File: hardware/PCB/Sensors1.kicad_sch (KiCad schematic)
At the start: 33 parts, among them J10 Conn_ACS712, U1 MCP6002T-I/SN, U102 INA333xxDGK, U201 QNHC3, U6 ACS712xLCTR-05B, U7 TLV431, U8 TLV431

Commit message: Rough Layout pcb
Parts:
- removed JP201: SolderJumper_2_Open, Jumper:SolderJumper-2_P1.3mm_Open_TrianglePad1.0x1.5mm, symbol Jumper:SolderJumper_2_Open
- removed U7: TLV431, Package_TO_SOT_SMD:SOT-23, symbol Reference_Voltage:REF3012
- added C202, C208: 100n, Capacitor_SMD:C_0805_2012Metric, symbol Device:C
- added R205, R213: 4.7k, Resistor_SMD:R_0805_2012Metric, symbol Device:R
- added TP201, TP202, TP203, TP204, TP205, TP206, TP207: TestPoint, TestPoint:TestPoint_Pad_D1.5mm, symbol Connector:TestPoint
- added U205: TLV431, Package_TO_SOT_SMD:SOT-23, symbol Reference_Voltage:REF3012
- C203: renamed from C9; JLCPCB Part (none) -> C28323; Link (none) -> https://jlcpcb.com/partdetail/29074-CL21B105KBFNNNE/C28323
- C209: renamed from C8; JLCPCB Part (none) -> C28323; Link (none) -> https://jlcpcb.com/partdetail/29074-CL21B105KBFNNNE/C28323
- J201: renamed from U203; value ~ -> ina333; footprint (none) -> footprints:board_ina333; Link (none) -> https://pl.aliexpress.com/item/1005006230563668.html?spm=a2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; now left out of the parts list
- J202: renamed from J10; value Conn_ACS712 -> ACS712; footprint (none) -> Connector_PinHeader_2.54mm:PinHeader_1x03_P2.54mm_Vertical; Link (none) -> https://pl.aliexpress.com/item/1005006207760044.html?spm=a2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; now left out of the parts list
- R202: renamed from R22; JLCPCB Part (none) -> C38522; Link (none) -> https://jlcpcb.com/partdetail/39505-0805W8F1002T5E/C38522
- R204: renamed from R12; now not fitted
- R206: renamed from R14; JLCPCB Part (none) -> C38522; Link (none) -> https://jlcpcb.com/partdetail/39505-0805W8F1002T5E/C38522
- R208: renamed from R25; JLCPCB Part (none) -> C38522; Link (none) -> https://jlcpcb.com/partdetail/39505-0805W8F1002T5E/C38522
- R211: renamed from R23; JLCPCB Part (none) -> C38522; Link (none) -> https://jlcpcb.com/partdetail/39505-0805W8F1002T5E/C38522
- R216: renamed from R20; JLCPCB Part (none) -> C38522; Link (none) -> https://jlcpcb.com/partdetail/39505-0805W8F1002T5E/C38522
- U201: renamed from U102; JLCPCB Part (none) -> C2057648; Link (none) -> https://jlcpcb.com/partdetail/TexasInstruments-INA333AIDGKT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; MFR Part (none) -> INA333AIDGKT; Manufacturer (none) -> Texas Instruments
- renumbered C7 to C201, C5 to C204, C6 to C205, C1 to C206, C3 to C207, C4 to C210, JP1 to JP202, R11 to R201, R9 to R203, R6 to R207, R10 to R209, R19 to R210, R16 to R212, R13 to R214, R17 to R215, R18 to R217, U1 to U202, U8 to U203, U201 to U204, U6 to U206
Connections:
- net +3V3: no longer J201.3 (3V3)
- net +5V: now also C206.2, J201.3 (3V3); no longer C206.1
- net ACS712_out: now also TP205.1
- net Current_offset_1V5: now also TP206.1, U205.2 (OUT)
- net Current_opamp_V+: no longer R210.2, R212.2, U202.6 (-)
- net GND: now also C203.1, C205.1, C206.1, R208.1, U201.5 (Ref), C202.2, C208.2, U205.3 (GND); no longer C203.2, C205.2, C206.2, R208.2
- net QNHC3_out: now also TP204.1
- net ina333_Vin-: now also C205.2; no longer C205.1
- net ina333_Vout: now also C202.1, R205.2, TP203.1; no longer R201.1, U202.1
- net ina333_Vout_5V: now also TP201.1
- net ina333_Vref: no longer U201.5 (Ref)
- net ina333_offset_2V48: now also C203.2, R206.2, U203.2 (OUT), TP202.1; no longer C203.1, R206.1, U203.1 (IN)
- net ina333_opamp_V+: no longer R201.2, R203.2, U202.2 (-)
- net at R214.2, R216.1: now also U205.1 (REF)
- net QNH_out renamed Current_Vout
- net Current_Vout: now also R213.1
- new net: R206.1, R208.2, U203.1 (REF)
- new net Current_opamp_V-: R210.2, R212.2, U202.6 (-)
- new net QNH_Vout: C208.1, R213.2, TP207.1
- new net ina333_Vout_: R201.1, R205.1, U202.1
- new net ina333_opamp_V-: R201.2, R203.2, U202.2 (-)
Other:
- moved on the sheet: C203, C205, C209, R201, R202, R203, R206, R207, R208, R209, R210, R211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

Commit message: pcb XL4015
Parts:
- C203, C209: Distributor https://jlcpcb.com/partdetail/29074-CL21B105KBFNNNE/C28323 -> (none)
- R202, R206, R208, R211, R216: Distributor https://jlcpcb.com/partdetail/18102-0805W8F1002T5E/C17414 -> (none); Link https://jlcpcb.com/partdetail/39505-0805W8F1002T5E/C38522 -> https://jlcpcb.com/partdetail/18102-0805W8F1002T5E/C17414
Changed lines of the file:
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@@
 			)
 		)
-		(property "Distributor" "https://jlcpcb.com/partdetail/18102-0805W8F1002T5E/C17414"
-			(at 171.45 39.37 0)
-			(effects
-				(font
-					(size 1.27 1.27)
-				)
-				(hide yes)
-			)
-		)
 		(property "MFR Part" "0805W8F1002T5E "
 			(at 171.45 39.37 0)
@@
 			)
 		)
-		(property "Link" "https://jlcpcb.com/partdetail/39505-0805W8F1002T5E/C38522"
+		(property "Link" "https://jlcpcb.com/partdetail/18102-0805W8F1002T5E/C17414"
 			(at 171.45 39.37 0)
 			(effects
@@
 			)
 		)
-		(property "Distributor" "https://jlcpcb.com/partdetail/18102-0805W8F1002T5E/C17414"
-			(at 160.02 30.48 0)
-			(effects
-				(font
-					(size 1.27 1.27)
-				)
-				(hide yes)
-			)
-		)
 		(property "MFR Part" "0805W8F1002T5E "
 			(at 160.02 30.48 0)
@@
 			)
 		)
-		(property "Link" "https://jlcpcb.com/partdetail/39505-0805W8F1002T5E/C38522"
+		(property "Link" "https://jlcpcb.com/partdetail/18102-0805W8F1002T5E/C17414"
 			(at 160.02 30.48 0)
 			(effects
@@
 			)
 		)
-		(property "Distributor" "https://jlcpcb.com/partdetail/18102-0805W8F1002T5E/C17414"
-			(at 160.02 97.79 0)
-			(effects
-				(font
-					(size 1.27 1.27)
-				)
-				(hide yes)
-			)
-		)
 		(property "MFR Part" "0805W8F1002T5E "
 			(at 160.02 97.79 0)
@@
 			)
 		)
-		(property "Link" "https://jlcpcb.com/partdetail/39505-0805W8F1002T5E/C38522"
+		(property "Link" "https://jlcpcb.com/partdetail/18102-0805W8F1002T5E/C17414"
 			(at 160.02 97.79 0)
 			(effects
@@
 			)
 		)
-		(property "Distributor" "https://jlcpcb.com/partdetail/29074-CL21B105KBFNNNE/C28323"
-			(at 180.34 113.03 0)
-			(effects
-				(font
-					(size 1.27 1.27)
-				)
-				(hide yes)
-			)
-		)
 		(property "MFR Part" "CL21B105KBFNNNE"
 			(at 180.34 113.03 0)
@@
 			)
 		)
-		(property "Distributor" "https://jlcpcb.com/partdetail/18102-0805W8F1002T5E/C17414"
-			(at 171.45 116.84 0)
-			(effects
-				(font
-					(size 1.27 1.27)
-				)
-				(hide yes)
-			)
-		)
 		(property "MFR Part" "0805W8F1002T5E "
 			(at 171.45 116.84 0)
@@
 			)
 		)
-		(property "Link" "https://jlcpcb.com/partdetail/39505-0805W8F1002T5E/C38522"
+		(property "Link" "https://jlcpcb.com/partdetail/18102-0805W8F1002T5E/C17414"
 			(at 171.45 116.84 0)
 			(effects
@@
 			)
 		)
-		(property "Distributor" "https://jlcpcb.com/partdetail/18102-0805W8F1002T5E/C17414"
-			(at 171.45 46.99 0)
-			(effects
-				(font
-					(size 1.27 1.27)
-				)
-				(hide yes)
-			)
-		)
 		(property "MFR Part" "0805W8F1002T5E "
 			(at 171.45 46.99 0)
@@
 			)
 		)
-		(property "Link" "https://jlcpcb.com/partdetail/39505-0805W8F1002T5E/C38522"
+		(property "Link" "https://jlcpcb.com/partdetail/18102-0805W8F1002T5E/C17414"
 			(at 171.45 46.99 0)
 			(effects
@@
 			(at 180.34 43.18 0)
 			(effects
-				(font
-					(size 1.27 1.27)
-				)
-				(hide yes)
-			)
-		)
-		(property "Distributor" "https://jlcpcb.com/partdetail/29074-CL21B105KBFNNNE/C28323"
-			(at 180.34 43.18 0)
-			(effects

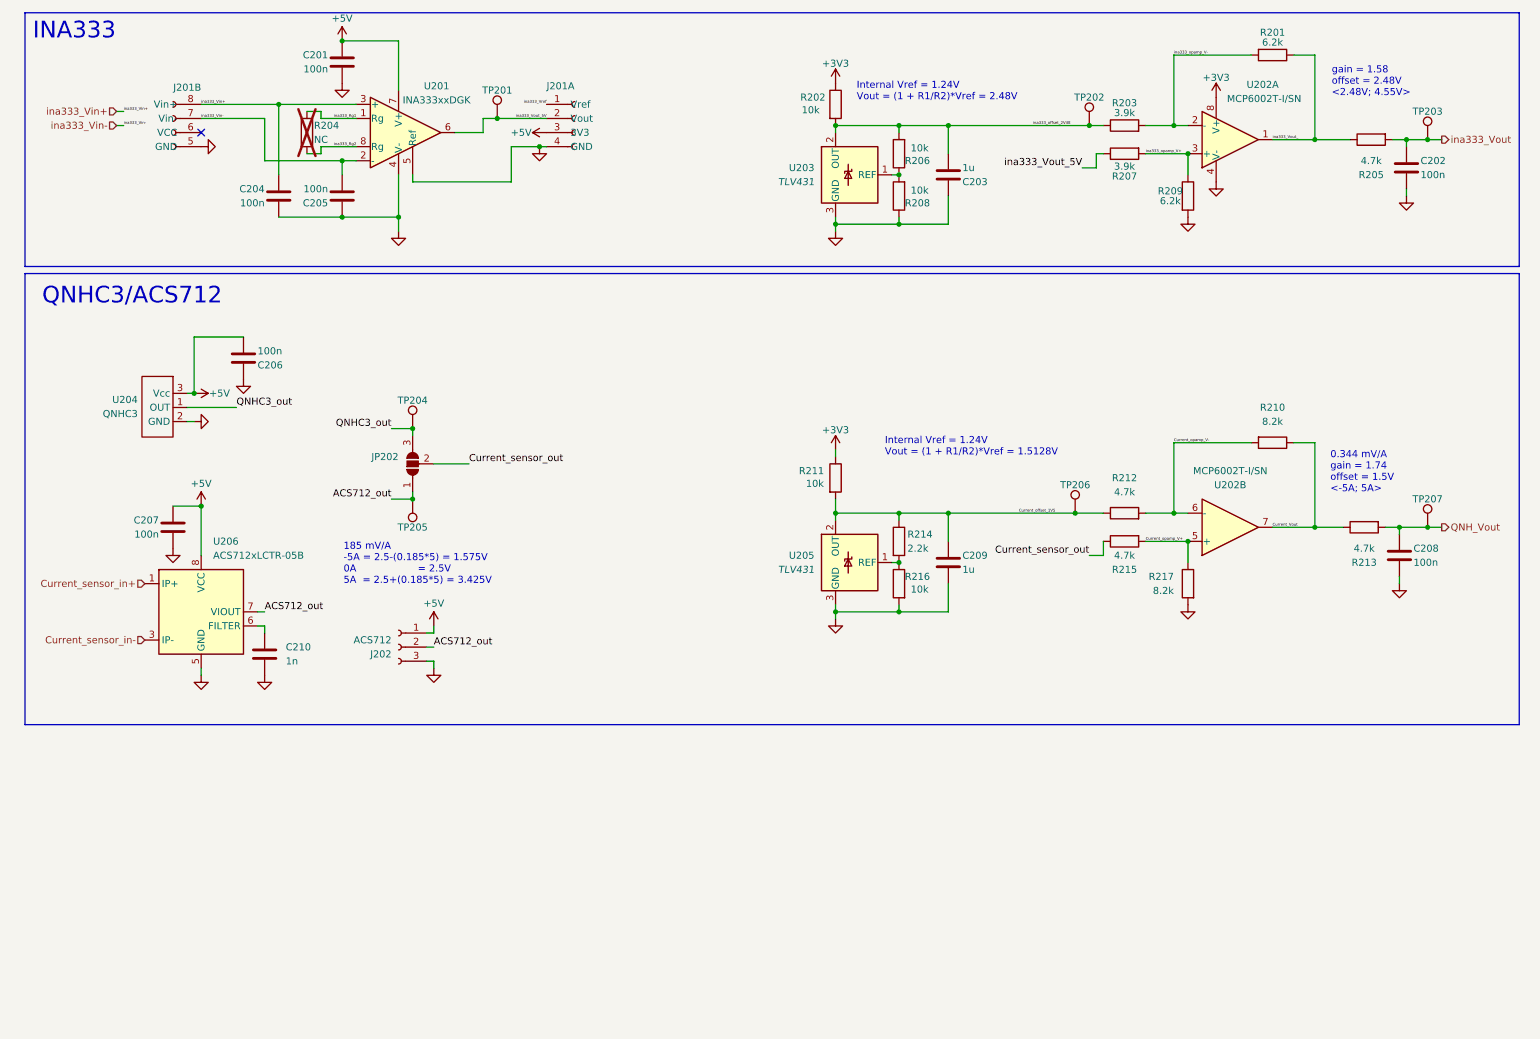
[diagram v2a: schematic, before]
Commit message: XL4015 CC, relays
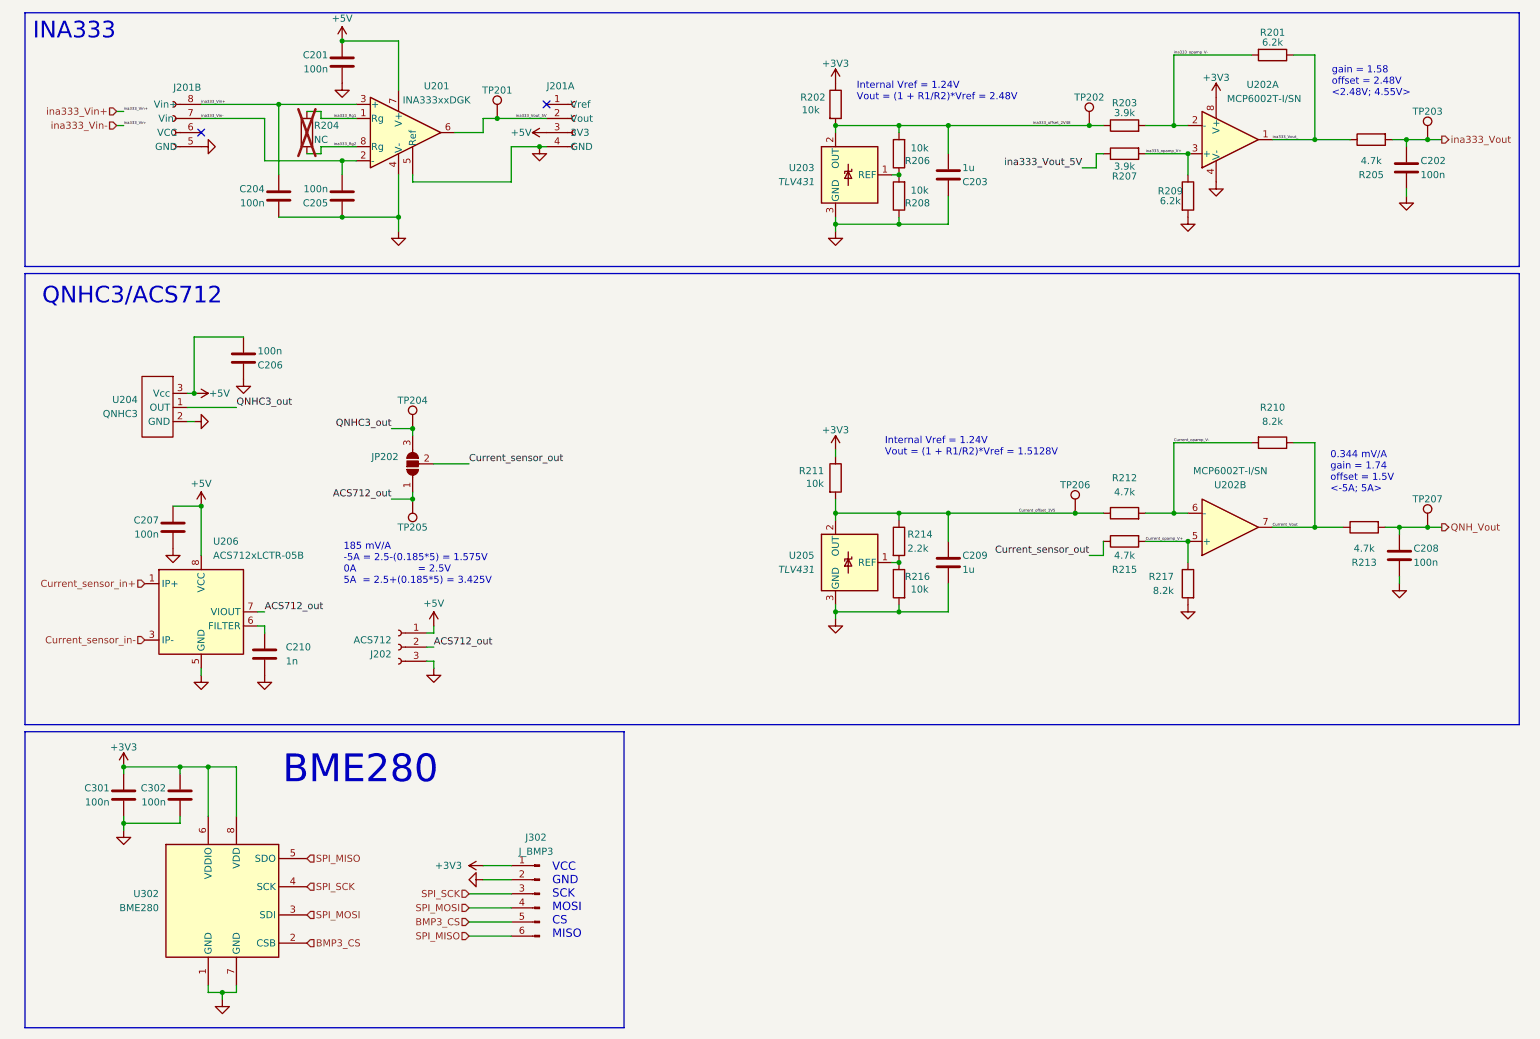
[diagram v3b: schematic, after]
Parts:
- added C301, C302: 100n, Capacitor_SMD:C_0805_2012Metric, symbol Device:C
- added J302: J_BMP3, Connector_JST:JST_XH_B6B-XH-A_1x06_P2.50mm_Vertical, symbol Connector:Conn_01x06_Pin
- added U302: BME280, Package_LGA:Bosch_LGA-8_2.5x2.5mm_P0.65mm_ClockwisePinNumbering, symbol Sensor:BME280
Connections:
- net +3V3: now also C301.1, C302.1, J302.1 (Pin_1), U302.6 (VDDIO), U302.8 (VDD)
- net GND: now also C301.2, C302.2, J302.2 (Pin_2), U302.1 (GND), U302.7 (GND)
- net ina333_Vref: no longer names the net of J201.1 (Vref)
- new net BMP3_CS: J302.5 (Pin_5), U302.2 (CSB)
- new net SPI_MISO: J302.6 (Pin_6), U302.5 (SDO)
- new net SPI_MOSI: J302.4 (Pin_4), U302.3 (SDI)
- new net SPI_SCK: J302.3 (Pin_3), U302.4 (SCK)
- no-connect marks 1 -> 2
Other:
- note added: "BME280"
- note added: "VCC GND SCK MOSI CS MISO"

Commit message: pcb
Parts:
- J202: now not fitted
- J203: renamed from J302; now not fitted
- TP201, TP202, TP203, TP204, TP205, TP206, TP207: footprint TestPoint:TestPoint_Pad_D1.5mm -> TestPoint:TestPoint_THTPad_D1.5mm_Drill0.7mm
- renumbered C301 to C211, C302 to C212, JP202 to JP201, U302 to U207
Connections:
- net Current_sensor_in+: now also U206.3 (IP-), U206.4 (IP-); no longer U206.1 (IP+), U206.2 (IP+)
- net Current_sensor_in-: now also U206.1 (IP+), U206.2 (IP+); no longer U206.3 (IP-), U206.4 (IP-)
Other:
- moved on the sheet: R202, R211

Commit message: PCB final routing
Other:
- company: (none) -> Authors: D. Ledzianowski K. Lewandowska T. Majchrzak
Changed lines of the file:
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@@
 	(generator_version "9.0")
 	(paper "A4")
+	(title_block
+		(date "2025-12-07")
+		(rev "1.0")
+		(company "Authors: D. Ledzianowski K. Lewandowska T. Majchrzak")
+	)
 	(rectangle
 		(start 13.97 60.96)

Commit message: PCB final design
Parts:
- removed C211, C212: 100n, Capacitor_SMD:C_0805_2012Metric, symbol Device:C
- removed U207: BME280, Package_LGA:Bosch_LGA-8_2.5x2.5mm_P0.65mm_ClockwisePinNumbering, symbol Sensor:BME280
- J201, U204: now not fitted
- J203: value J_BMP3 -> BMP3; footprint Connector_JST:JST_XH_B6B-XH-A_1x06_P2.50mm_Vertical -> Connector_PinHeader_2.54mm:PinHeader_1x06_P2.54mm_Vertical; JLCPCB Part C2337 -> (none); Link https://pl.aliexpress.com/item/1005006960863510.html?spm=a2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 -> (none)
- R201, R209, R210, R214, R217: Manufacturer UNI-ROYAL(Uniroyal Elec) -> UNI-ROYAL(Uniroyal Elec)
- R202, R206, R208, R211, R216: JLCPCB Part C38522 -> C17414; MFR Part 0805W8F1002T5E -> 0805W8F1002T5E; Manufacturer UNI-ROYAL(Uniroyal Elec) -> UNI-ROYAL(Uniroyal Elec)
- R203, R207: JLCPCB Part C17614 -> C17614; MFR Part 0805W8F3901T5E -> 0805W8F3901T5E; Manufacturer UNI-ROYAL(Uniroyal Elec) -> UNI-ROYAL(Uniroyal Elec)
- R205, R212, R213, R215: MFR Part 0805W8F4701T5E -> 0805W8F4701T5E; Manufacturer UNI-ROYAL(Uniroyal Elec) -> UNI-ROYAL(Uniroyal Elec)
- U202: JLCPCB Part C7377 -> C7377; Manufacturer Microchip Tech -> Microchip Tech
- U206: JLCPCB Part C44471 -> C44471; Manufacturer Allegro MicroSystems, LLC -> Allegro MicroSystems, LLC
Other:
- moved on the sheet: J203

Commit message: usb, sd
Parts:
- J201, J202, J203, R204, U204: now fitted
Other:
- note added: "ACS712"
- note added: "QNHC3"
- note removed: "QNHC3/ACS712"
- title: (none) -> Stanowisko do badania parametrów pracy ogniw Li-Ion Li-Pol
- moved on the sheet: C201, C202, C203, C204, C205, C206, C207, C208, C209, C210, JP201, R201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
